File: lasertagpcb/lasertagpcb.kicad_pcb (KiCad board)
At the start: 2 copper layers, 74 x 32 mm, 29 parts, among them J1 Conn_01x04_Socket, J2 Conn_01x02, J3 Conn_01x02_Socket, Q1 VN2106, U1 MCP6002-xP

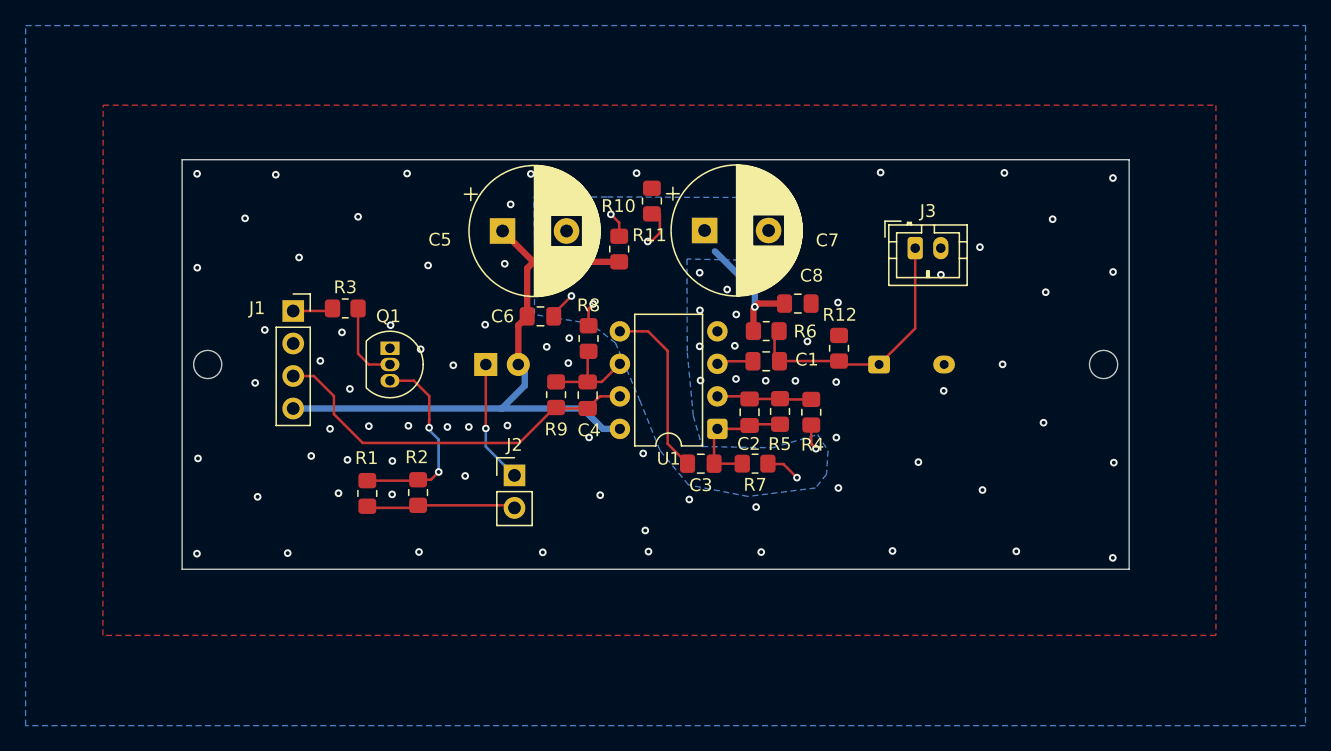
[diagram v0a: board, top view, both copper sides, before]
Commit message: updated photo diode
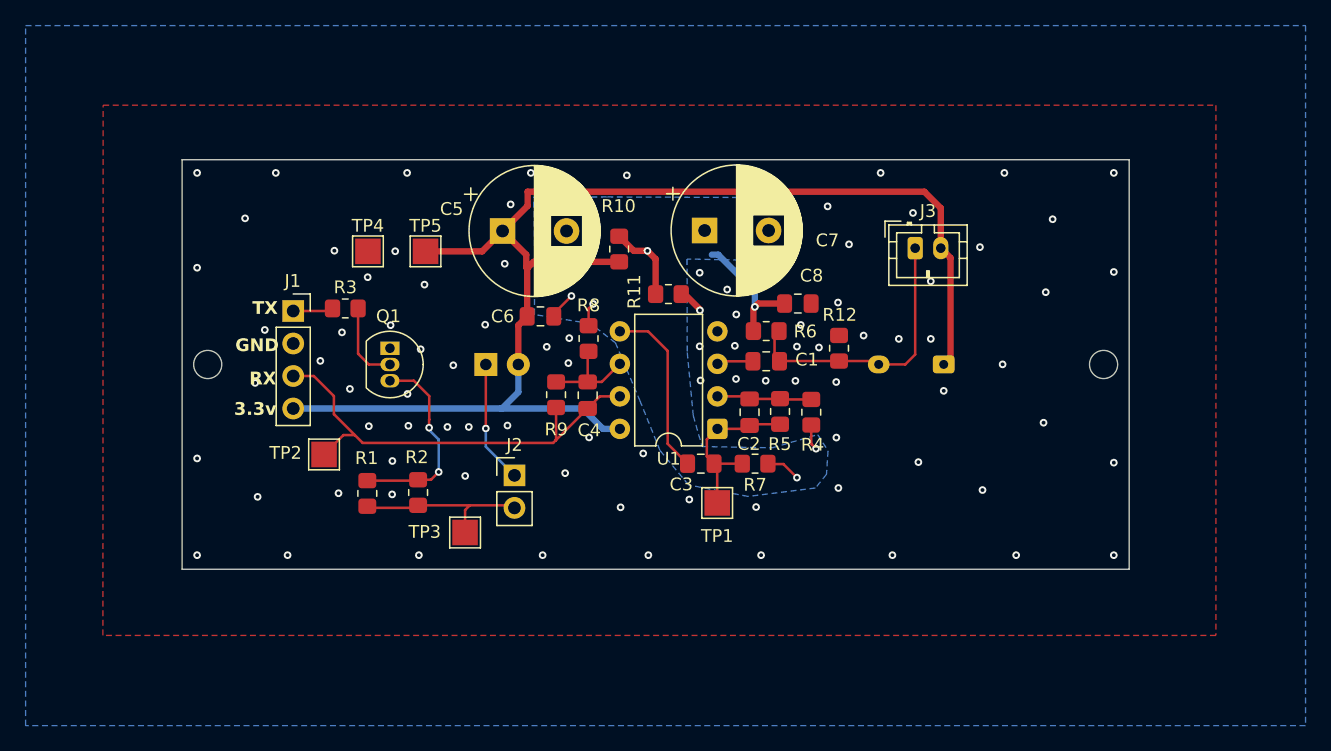
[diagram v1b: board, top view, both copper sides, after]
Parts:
- added TP1: TestPoint, TestPoint:TestPoint_Pad_2.0x2.0mm, F.Cu at (138.8, 83.8)
- added TP2: TestPoint, TestPoint:TestPoint_Pad_2.0x2.0mm, F.Cu at (108.1, 80.0)
- added TP3: TestPoint, TestPoint:TestPoint_Pad_2.0x2.0mm, F.Cu at (119.1, 86.1)
- added TP4: TestPoint, TestPoint:TestPoint_Pad_2.0x2.0mm, F.Cu at (111.5, 64.2)
- added TP5: TestPoint, TestPoint:TestPoint_Pad_2.0x2.0mm, F.Cu at (116.0, 64.2)
- moved R11 7.38 mm to (135.0, 67.5), turned to 180 degrees
- moved D2 5.05 mm to (156.5, 73.0), turned to 180 degrees
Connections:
- D2 pad 1: /sigin -> +3V3
- D2 pad 2: GND -> /sigin
- J3 pad 2: GND -> +3V3
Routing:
- net +3V3: track 49.1 -> 105.3 mm
- net /Rx: track 30.1 -> 35.7 mm
- net Net-(C2-Pad2): track 10.1 -> 13.7 mm
- net Net-(J2-Pin_2): track 11.7 -> 14.0 mm
- net GND: track 0.00 -> 2.07 mm, vias 85 -> 92
- net /a_gnd: track 23.4 -> 25.2 mm, vias 7 -> 6
- net /sigin: track 20.8 -> 22.4 mm
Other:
- board text added: "3.3v"
- board text added: "GND"
- board text added: "RX"
- board text added: "TX"

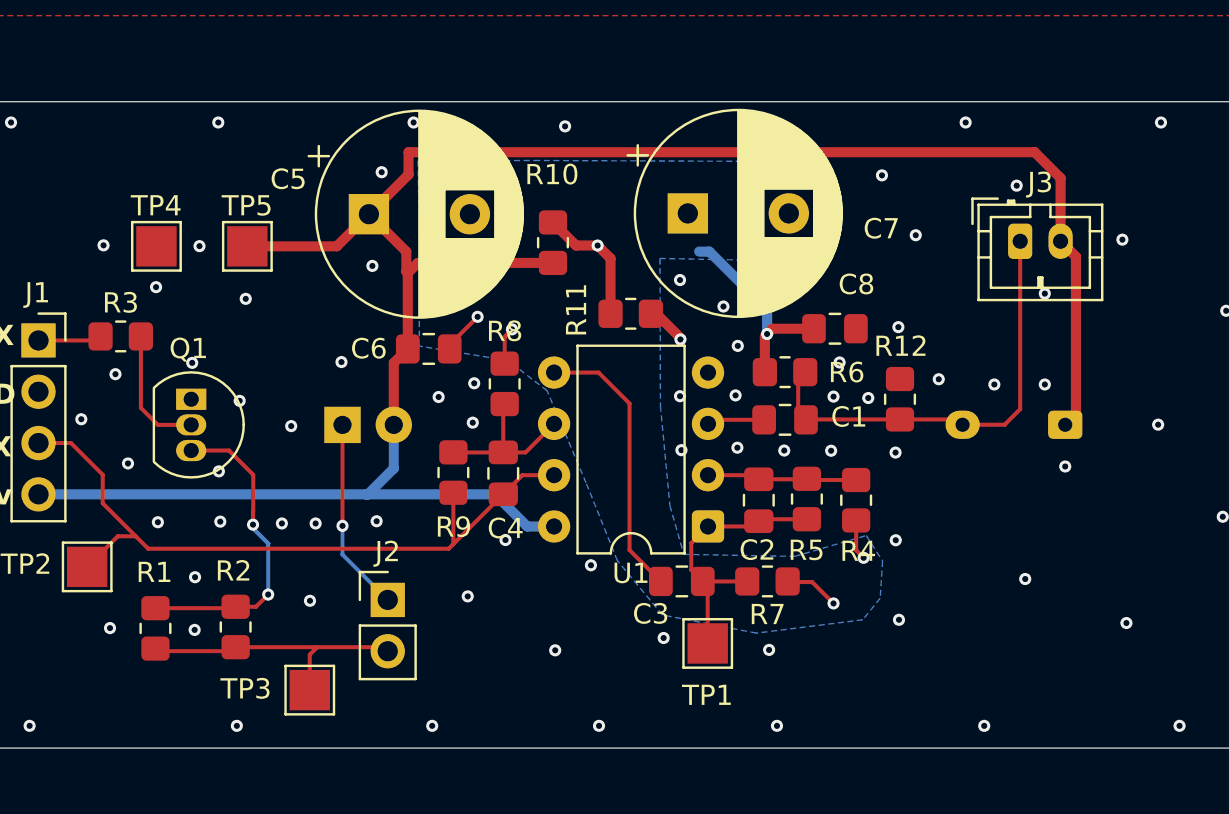
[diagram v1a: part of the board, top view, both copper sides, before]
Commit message: Updated layout. Added decoupling caps
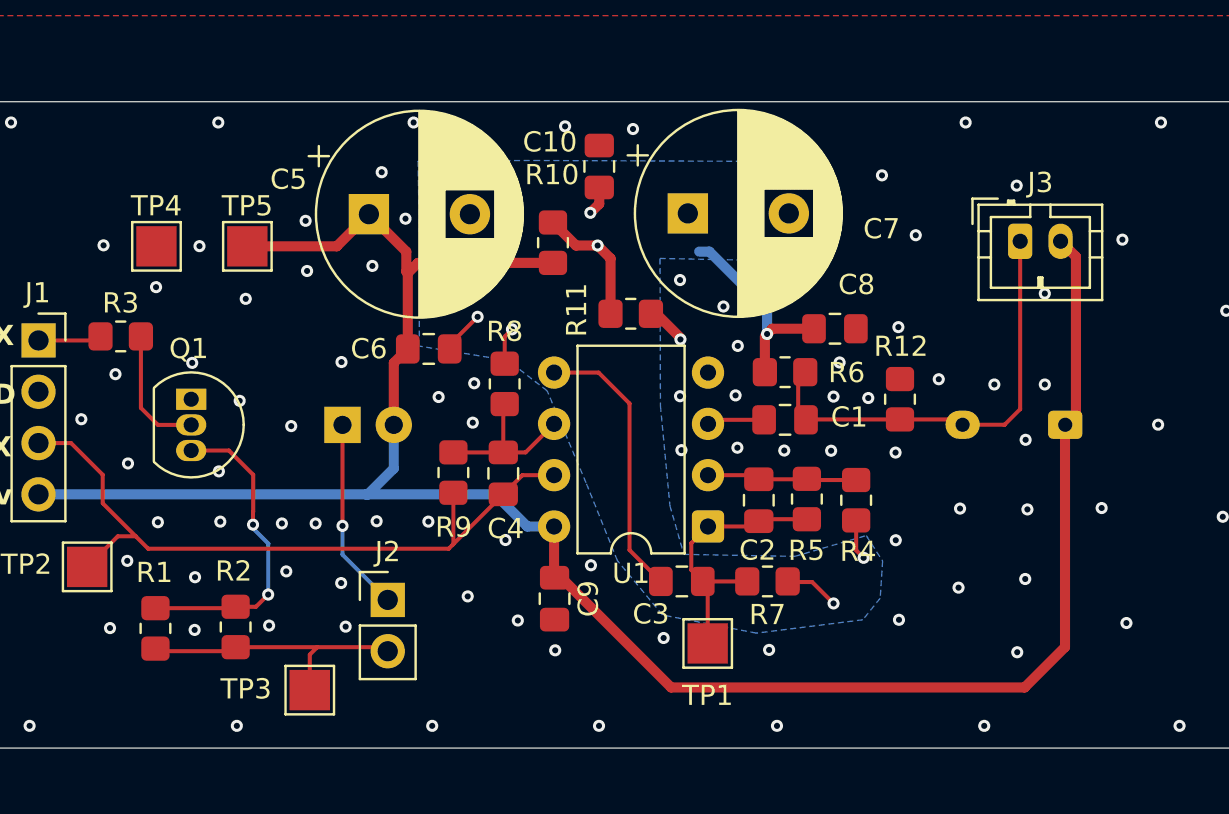
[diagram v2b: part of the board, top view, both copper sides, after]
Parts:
- added C10: 100 nF, Capacitor_SMD:C_0805_2012Metric_Pad1.18x1.45mm_HandSolder, F.Cu at (133.4, 60.2)
- added C9: 100 nF, Capacitor_SMD:C_0805_2012Metric_Pad1.18x1.45mm_HandSolder, F.Cu at (131.2, 81.6)
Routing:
- net +3V3: track 105.3 -> 107.4 mm
- net /a_gnd: track 25.2 -> 26.6 mm, vias 6 -> 7
- net GND: vias 92 -> 107
